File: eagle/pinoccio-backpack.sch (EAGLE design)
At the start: 2 parts

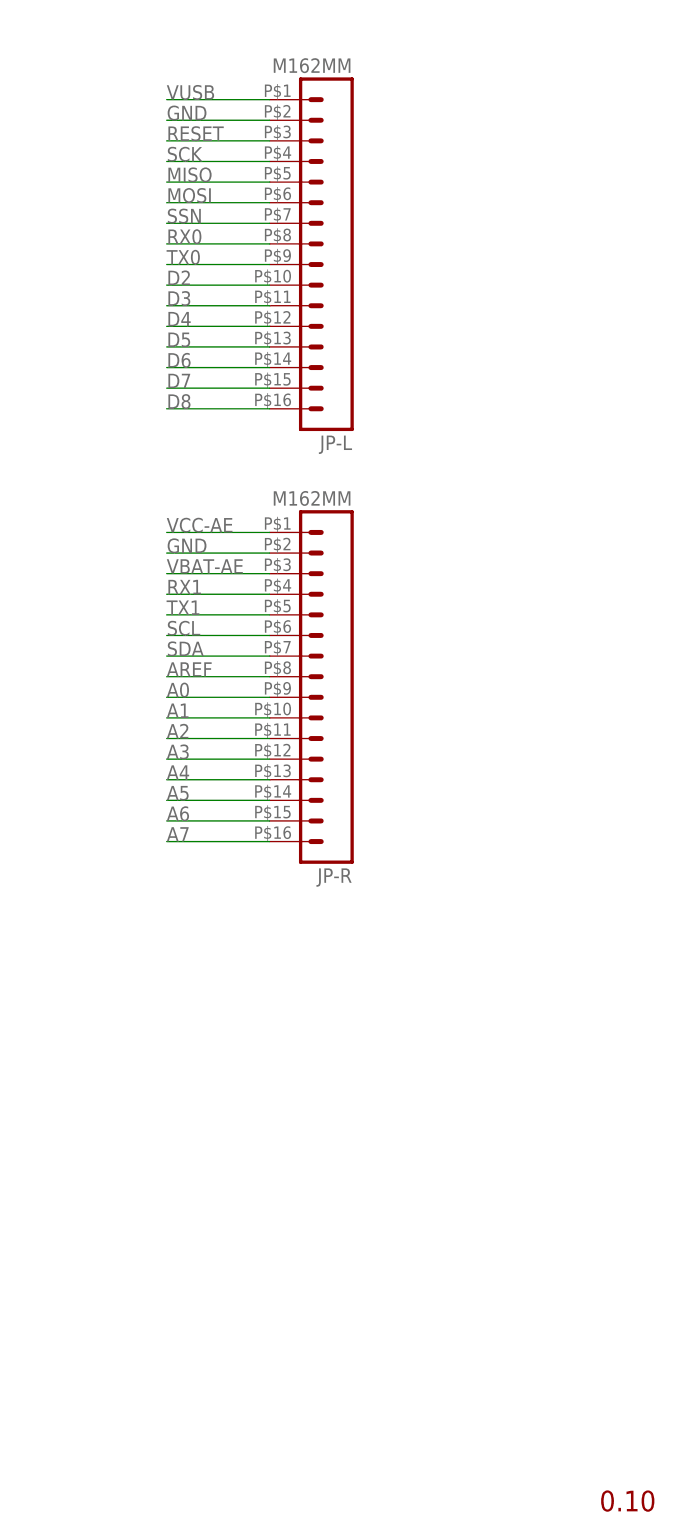
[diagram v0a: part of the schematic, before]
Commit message: Updated backpack reference spec
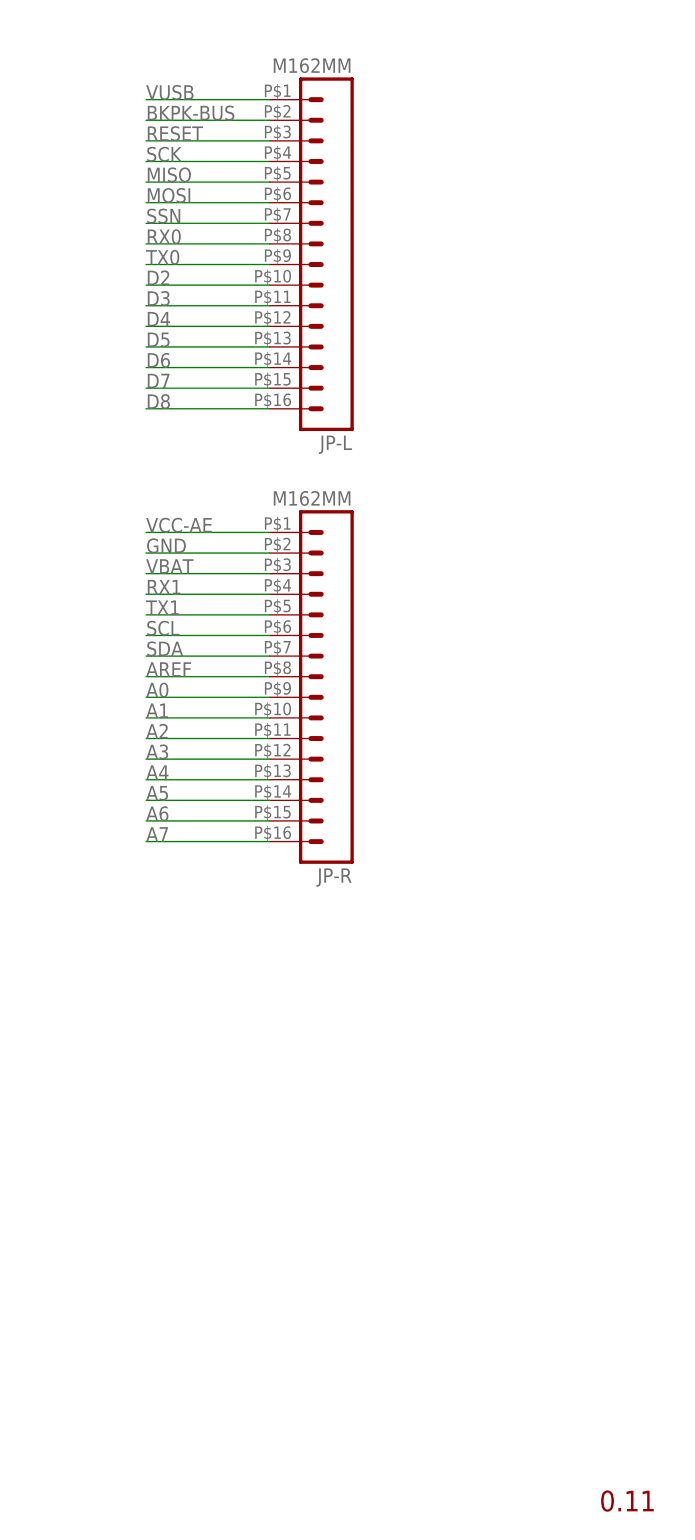
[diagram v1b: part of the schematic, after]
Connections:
- net VBAT-AE renamed VBAT
- new net BKPK-BUS: JP-L.2
- net GND: no longer JP-L.2
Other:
- note added: "0.11"
- note removed: "0.10"

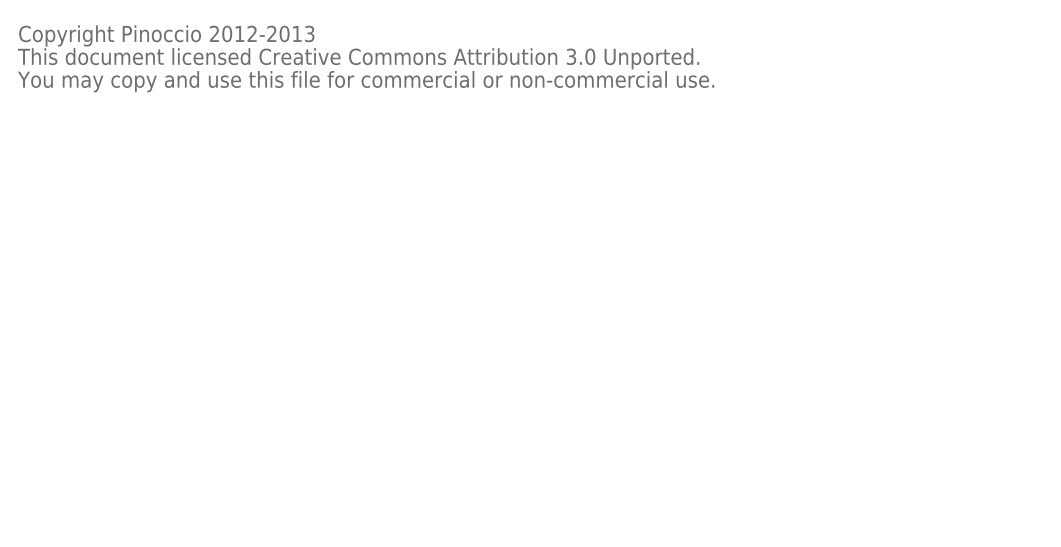
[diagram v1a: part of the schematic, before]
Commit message: Add ATtiny13 support for backpack bus
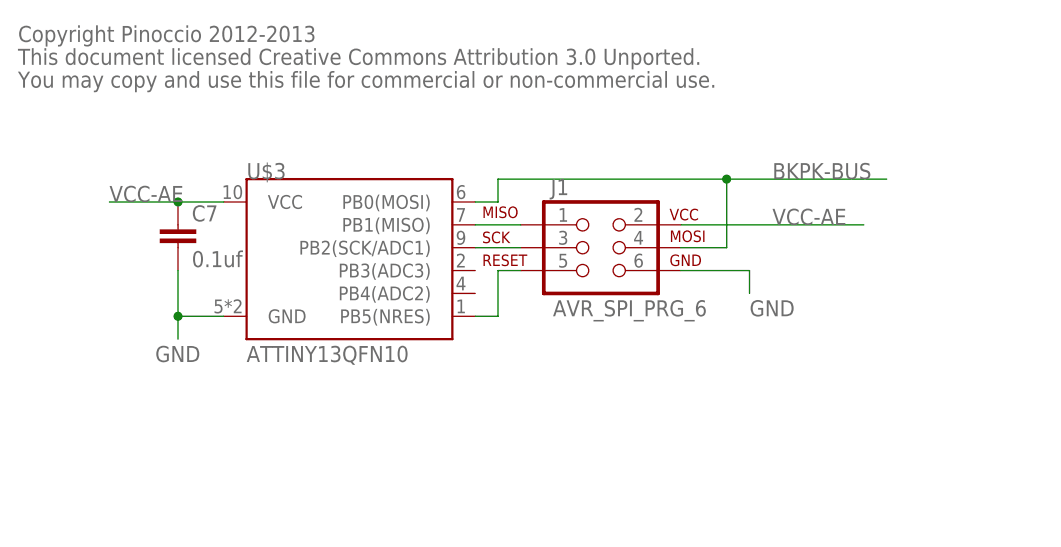
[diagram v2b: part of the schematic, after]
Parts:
- added C7: 0.1uf, Pinoccio:CAP0402-CAP
- added J1: AVR_SPI_PRG_6, Pinoccio:AVR_SPI_PRG_6
- added U$3: ATTINY13QFN10, Pinoccio:ATTINY13QFN10
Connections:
- new net N$2: J1.1, U$3.PB1(MISO)
- new net N$3: J1.3, U$3.PB2(SCK/ADC1)
- new net N$4: J1.5, U$3.PB5(NRES)
- net BKPK-BUS: now also J1.4, U$3.PB0(MOSI)
- net GND: now also C7.2, J1.6, U$3.GND
- net VCC-AE: now also C7.1, J1.2, U$3.VCC
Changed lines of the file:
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@@
 <part name="JP-R" library="Pinoccio" deviceset="M16" device="2MM"/>
 <part name="JP-L" library="Pinoccio" deviceset="M16" device="2MM"/>
+<part name="U$3" library="Pinoccio" deviceset="ATTINY13" device="QFN10"/>
+<part name="J1" library="Pinoccio" deviceset="AVR_SPI_PRG_6" device=""/>
+<part name="C7" library="Pinoccio" deviceset="CAP" device="0402-CAP" value="0.1uf"/>
 </parts>
 <sheets>
@@
 <instance part="JP-R" gate="G$1" x="208.28" y="101.6" rot="R180"/>
 <instance part="JP-L" gate="G$1" x="208.28" y="154.94" rot="R180"/>
+<instance part="U$3" gate="G$1" x="40.64" y="157.48"/>
+<instance part="J1" gate="G$1" x="66.04" y="160.02"/>
+<instance part="C7" gate="G$1" x="20.32" y="160.02"/>
 </instances>
 <busses>
@@
 <label x="182.88" y="119.38" size="1.778" layer="95"/>
 </segment>
+<segment>
+<pinref part="U$3" gate="G$1" pin="GND"/>
+<wire x1="25.4" y1="152.4" x2="20.32" y2="152.4" width="0.1524" layer="91"/>
+<wire x1="20.32" y1="152.4" x2="20.32" y2="149.86" width="0.1524" layer="91"/>
+<label x="17.78" y="147.32" size="1.778" layer="95"/>
+<pinref part="C7" gate="G$1" pin="2"/>
+<wire x1="20.32" y1="157.48" x2="20.32" y2="152.4" width="0.1524" layer="91"/>
+<junction x="20.32" y="152.4"/>
+</segment>
+<segment>
+<pinref part="J1" gate="G$1" pin="6"/>
+<wire x1="76.2" y1="157.48" x2="83.82" y2="157.48" width="0.1524" layer="91"/>
+<wire x1="83.82" y1="157.48" x2="83.82" y2="154.94" width="0.1524" layer="91"/>
+<label x="83.82" y="152.4" size="1.778" layer="95"/>
+</segment>
 </net>
 <net name="MOSI" class="0">
@@
 <label x="182.88" y="121.92" size="1.778" layer="95"/>
 </segment>
+<segment>
+<pinref part="U$3" gate="G$1" pin="VCC"/>
+<wire x1="25.4" y1="165.1" x2="20.32" y2="165.1" width="0.1524" layer="91"/>
+<label x="12.7" y="165.1" size="1.778" layer="95"/>
+<pinref part="C7" gate="G$1" pin="1"/>
+<wire x1="20.32" y1="165.1" x2="12.7" y2="165.1" width="0.1524" layer="91"/>
+<junction x="20.32" y="165.1"/>
+</segment>
+<segment>
+<pinref part="J1" gate="G$1" pin="2"/>
+<wire x1="76.2" y1="162.56" x2="96.52" y2="162.56" width="0.1524" layer="91"/>
+<label x="86.36" y="162.56" size="1.778" layer="95"/>
+</segment>
 </net>
 <net name="D2" class="0">
@@
 <label x="182.88" y="172.72" size="1.778" layer="95"/>
 </segment>
+<segment>
+<pinref part="J1" gate="G$1" pin="4"/>
+<wire x1="76.2" y1="160.02" x2="81.28" y2="160.02" width="0.1524" layer="91"/>
+<wire x1="81.28" y1="160.02" x2="81.28" y2="167.64" width="0.1524" layer="91"/>
+<pinref part="U$3" gate="G$1" pin="PB0(MOSI)"/>
+<wire x1="81.28" y1="167.64" x2="55.88" y2="167.64" width="0.1524" layer="91"/>
+<wire x1="55.88" y1="167.64" x2="55.88" y2="165.1" width="0.1524" layer="91"/>
+<wire x1="55.88" y1="165.1" x2="53.34" y2="165.1" width="0.1524" layer="91"/>
+<wire x1="81.28" y1="167.64" x2="99.06" y2="167.64" width="0.1524" layer="91"/>
+<junction x="81.28" y="167.64"/>
+<label x="86.36" y="167.64" size="1.778" layer="95"/>
+</segment>
 </net>
 <net name="VBAT" class="0">
@@
 </segment>
 </net>
+<net name="N$2" class="0">
+<segment>
+<pinref part="J1" gate="G$1" pin="1"/>
+<pinref part="U$3" gate="G$1" pin="PB1(MISO)"/>
+<wire x1="58.42" y1="162.56" x2="53.34" y2="162.56" width="0.1524" layer="91"/>
+</segment>
+</net>
+<net name="N$3" class="0">
+<segment>
+<pinref part="J1" gate="G$1" pin="3"/>
+<pinref part="U$3" gate="G$1" pin="PB2(SCK/ADC1)"/>
+<wire x1="58.42" y1="160.02" x2="53.34" y2="160.02" width="0.1524" layer="91"/>
+</segment>
+</net>
+<net name="N$4" class="0">
+<segment>
+<pinref part="J1" gate="G$1" pin="5"/>
+<wire x1="58.42" y1="157.48" x2="55.88" y2="157.48" width="0.1524" layer="91"/>
+<wire x1="55.88" y1="157.48" x2="55.88" y2="152.4" width="0.1524" layer="91"/>
+<pinref part="U$3" gate="G$1" pin="PB5(NRES)"/>
+<wire x1="55.88" y1="152.4" x2="53.34" y2="152.4" width="0.1524" layer="91"/>
+</segment>
+</net>

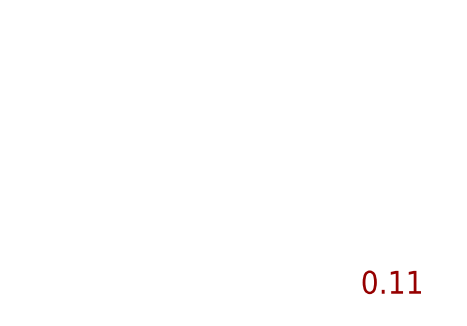
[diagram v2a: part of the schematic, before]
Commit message: Updated to v0.13 layout to match latest header location changes
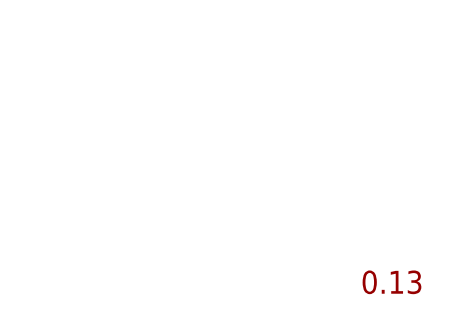
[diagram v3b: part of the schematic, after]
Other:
- note added: "0.13"
- note removed: "0.11"
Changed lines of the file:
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@@
 <sheet>
 <plain>
-<text x="238.76" y="1.27" size="2.54" layer="94" font="vector">0.11</text>
+<text x="238.76" y="1.27" size="2.54" layer="94" font="vector">0.13</text>
 <rectangle x1="0.38735" y1="0.29845" x2="0.41275" y2="0.31115" layer="21"/>
 <rectangle x1="0.36195" y1="0.31115" x2="0.45085" y2="0.32385" layer="21"/>

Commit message: Version 1.0
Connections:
- removed net N$2: J1.1, U$3.PB1(MISO)
- new net N$1: J1.4, U$3.PB0(MOSI)
- net BKPK-BUS: now also J1.1, U$3.PB1(MISO); no longer J1.4, U$3.PB0(MOSI)
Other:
- note added: "1.0"
- note removed: "0.13"
- moved on the sheet: JP-L, JP-R

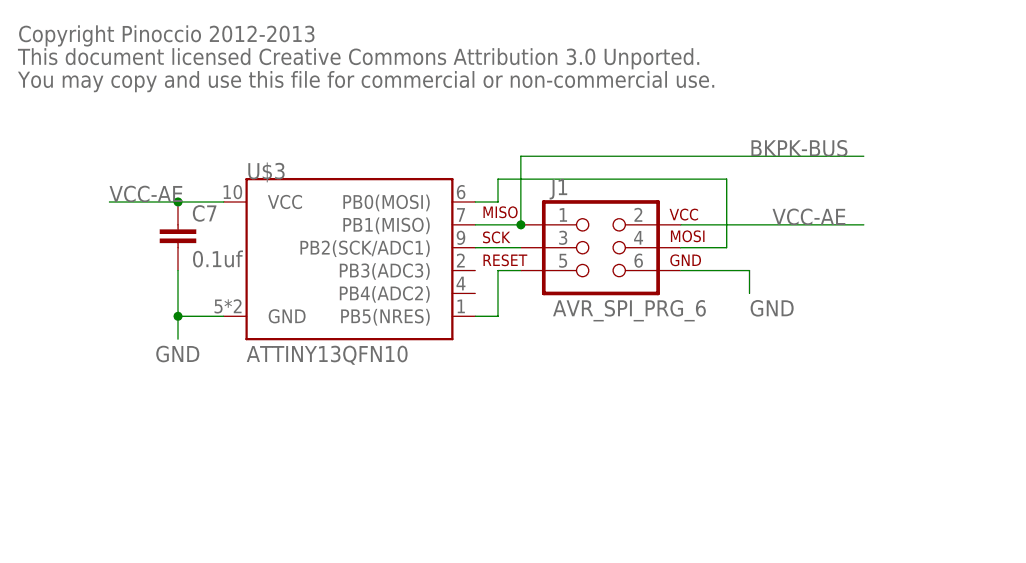
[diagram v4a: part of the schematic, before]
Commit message: Added reset pull-up to tiny13
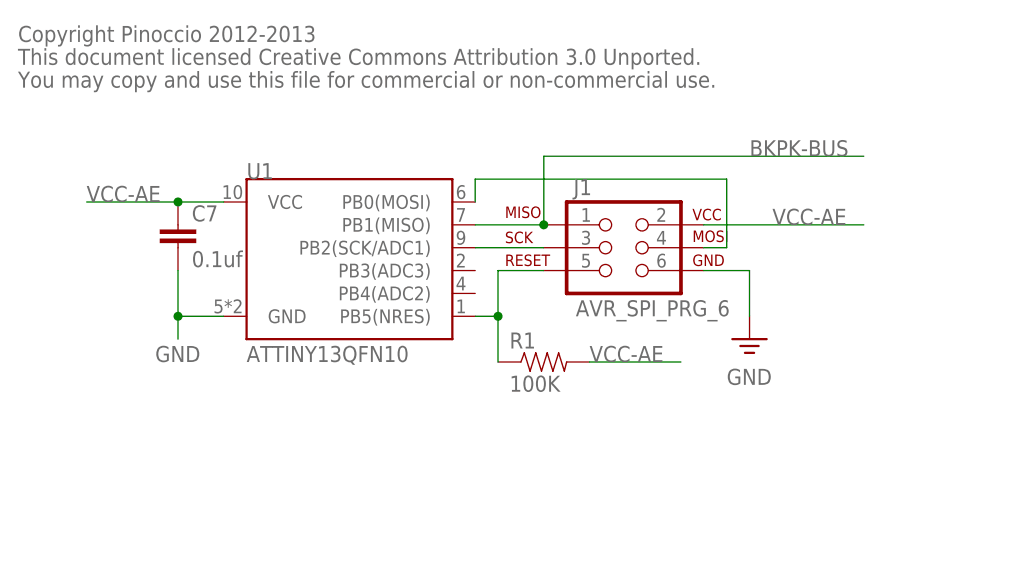
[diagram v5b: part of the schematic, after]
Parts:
- added R1: 100K, Pinoccio:RESISTOR0402-RES
- renumbered U$3 to U1
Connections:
- net N$4: now also R1.1
- net VCC-AE: now also R1.2
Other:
- moved on the sheet: J1
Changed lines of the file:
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@@
 <part name="JP-R" library="Pinoccio" deviceset="M16" device="2MM"/>
 <part name="JP-L" library="Pinoccio" deviceset="M16" device="2MM"/>
-<part name="U$3" library="Pinoccio" deviceset="ATTINY13" device="QFN10"/>
+<part name="U1" library="Pinoccio" deviceset="ATTINY13" device="QFN10"/>
 <part name="J1" library="Pinoccio" deviceset="AVR_SPI_PRG_6" device=""/>
 <part name="C7" library="Pinoccio" deviceset="CAP" device="0402-CAP" value="0.1uf"/>
+<part name="GND1" library="Pinoccio" deviceset="GND" device=""/>
+<part name="R1" library="Pinoccio" deviceset="RESISTOR" device="0402-RES" value="100K"/>
 </parts>
 <sheets>
@@
 <instance part="JP-R" gate="G$1" x="241.3" y="101.6" rot="R180"/>
 <instance part="JP-L" gate="G$1" x="241.3" y="154.94" rot="R180"/>
-<instance part="U$3" gate="G$1" x="40.64" y="157.48"/>
-<instance part="J1" gate="G$1" x="66.04" y="160.02"/>
+<instance part="U1" gate="G$1" x="40.64" y="157.48"/>
+<instance part="J1" gate="G$1" x="68.58" y="160.02"/>
 <instance part="C7" gate="G$1" x="20.32" y="160.02"/>
+<instance part="GND1" gate="1" x="83.82" y="149.86"/>
+<instance part="R1" gate="G$1" x="60.96" y="147.32"/>
 </instances>
 <busses>
@@
 </segment>
 <segment>
-<pinref part="U$3" gate="G$1" pin="GND"/>
+<pinref part="U1" gate="G$1" pin="GND"/>
 <wire x1="25.4" y1="152.4" x2="20.32" y2="152.4" width="0.1524" layer="91"/>
 <wire x1="20.32" y1="152.4" x2="20.32" y2="149.86" width="0.1524" layer="91"/>
@@
 <segment>
 <pinref part="J1" gate="G$1" pin="6"/>
-<wire x1="76.2" y1="157.48" x2="83.82" y2="157.48" width="0.1524" layer="91"/>
-<wire x1="83.82" y1="157.48" x2="83.82" y2="154.94" width="0.1524" layer="91"/>
-<label x="83.82" y="152.4" size="1.778" layer="95"/>
+<wire x1="78.74" y1="157.48" x2="83.82" y2="157.48" width="0.1524" layer="91"/>
+<wire x1="83.82" y1="157.48" x2="83.82" y2="152.4" width="0.1524" layer="91"/>
+<pinref part="GND1" gate="1" pin="GND"/>
 </segment>
 </net>
@@
 </segment>
 <segment>
-<pinref part="U$3" gate="G$1" pin="VCC"/>
+<pinref part="U1" gate="G$1" pin="VCC"/>
 <wire x1="25.4" y1="165.1" x2="20.32" y2="165.1" width="0.1524" layer="91"/>
-<label x="12.7" y="165.1" size="1.778" layer="95"/>
+<label x="10.16" y="165.1" size="1.778" layer="95"/>
 <pinref part="C7" gate="G$1" pin="1"/>
-<wire x1="20.32" y1="165.1" x2="12.7" y2="165.1" width="0.1524" layer="91"/>
+<wire x1="20.32" y1="165.1" x2="10.16" y2="165.1" width="0.1524" layer="91"/>
 <junction x="20.32" y="165.1"/>
 </segment>
 <segment>
 <pinref part="J1" gate="G$1" pin="2"/>
-<wire x1="76.2" y1="162.56" x2="96.52" y2="162.56" width="0.1524" layer="91"/>
+<wire x1="78.74" y1="162.56" x2="96.52" y2="162.56" width="0.1524" layer="91"/>
 <label x="86.36" y="162.56" size="1.778" layer="95"/>
 </segment>
+<segment>
+<pinref part="R1" gate="G$1" pin="2"/>
+<wire x1="66.04" y1="147.32" x2="76.2" y2="147.32" width="0.1524" layer="91"/>
+<label x="66.04" y="147.32" size="1.778" layer="95"/>
+</segment>
 </net>
 <net name="D2" class="0">
@@
 <segment>
 <pinref part="J1" gate="G$1" pin="1"/>
-<pinref part="U$3" gate="G$1" pin="PB1(MISO)"/>
-<wire x1="58.42" y1="162.56" x2="53.34" y2="162.56" width="0.1524" layer="91"/>
-<wire x1="58.42" y1="162.56" x2="58.42" y2="170.18" width="0.1524" layer="91"/>
-<wire x1="58.42" y1="170.18" x2="96.52" y2="170.18" width="0.1524" layer="91"/>
-<junction x="58.42" y="162.56"/>
+<pinref part="U1" gate="G$1" pin="PB1(MISO)"/>
+<wire x1="60.96" y1="162.56" x2="53.34" y2="162.56" width="0.1524" layer="91"/>
+<wire x1="60.96" y1="162.56" x2="60.96" y2="170.18" width="0.1524" layer="91"/>
+<wire x1="60.96" y1="170.18" x2="96.52" y2="170.18" width="0.1524" layer="91"/>
+<junction x="60.96" y="162.56"/>
 <label x="83.82" y="170.18" size="1.778" layer="95"/>
 </segment>
@@
 <segment>
 <pinref part="J1" gate="G$1" pin="3"/>
-<pinref part="U$3" gate="G$1" pin="PB2(SCK/ADC1)"/>
-<wire x1="58.42" y1="160.02" x2="53.34" y2="160.02" width="0.1524" layer="91"/>
+<pinref part="U1" gate="G$1" pin="PB2(SCK/ADC1)"/>
+<wire x1="60.96" y1="160.02" x2="53.34" y2="160.02" width="0.1524" layer="91"/>
 </segment>
 </net>
@@
 <segment>
 <pinref part="J1" gate="G$1" pin="5"/>
-<wire x1="58.42" y1="157.48" x2="55.88" y2="157.48" width="0.1524" layer="91"/>
+<wire x1="60.96" y1="157.48" x2="55.88" y2="157.48" width="0.1524" layer="91"/>
 <wire x1="55.88" y1="157.48" x2="55.88" y2="152.4" width="0.1524" layer="91"/>
-<pinref part="U$3" gate="G$1" pin="PB5(NRES)"/>
+<pinref part="U1" gate="G$1" pin="PB5(NRES)"/>
 <wire x1="55.88" y1="152.4" x2="53.34" y2="152.4" width="0.1524" layer="91"/>
+<pinref part="R1" gate="G$1" pin="1"/>
+<wire x1="55.88" y1="152.4" x2="55.88" y2="147.32" width="0.1524" layer="91"/>
+<junction x="55.88" y="152.4"/>
 </segment>
 </net>
@@
 <segment>
 <pinref part="J1" gate="G$1" pin="4"/>
-<wire x1="76.2" y1="160.02" x2="81.28" y2="160.02" width="0.1524" layer="91"/>
-<pinref part="U$3" gate="G$1" pin="PB0(MOSI)"/>
-<wire x1="53.34" y1="165.1" x2="55.88" y2="165.1" width="0.1524" layer="91"/>
-<wire x1="55.88" y1="165.1" x2="55.88" y2="167.64" width="0.1524" layer="91"/>
-<wire x1="55.88" y1="167.64" x2="81.28" y2="167.64" width="0.1524" layer="91"/>
+<wire x1="78.74" y1="160.02" x2="81.28" y2="160.02" width="0.1524" layer="91"/>
+<pinref part="U1" gate="G$1" pin="PB0(MOSI)"/>
+<wire x1="53.34" y1="165.1" x2="53.34" y2="167.64" width="0.1524" layer="91"/>
+<wire x1="53.34" y1="167.64" x2="81.28" y2="167.64" width="0.1524" layer="91"/>
 <wire x1="81.28" y1="167.64" x2="81.28" y2="160.02" width="0.1524" layer="91"/>
 </segment>
